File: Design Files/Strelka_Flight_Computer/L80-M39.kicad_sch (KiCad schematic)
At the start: 15 parts

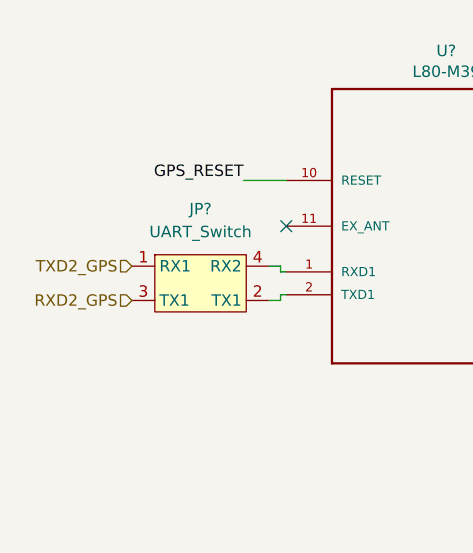
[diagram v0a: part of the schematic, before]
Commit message: Pin mapping and created STM32 .ioc for reference
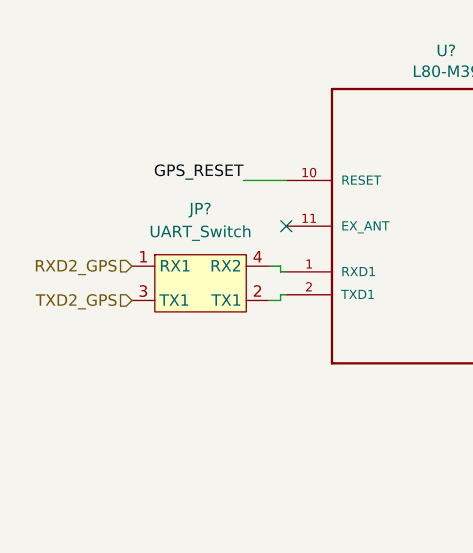
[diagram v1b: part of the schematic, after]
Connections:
- net RXD2_GPS: now also JP?.1 (RX1); no longer JP?.3 (TX1)
- net TXD2_GPS: now also JP?.3 (TX1); no longer JP?.1 (RX1)
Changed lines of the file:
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@@
     (effects (font (size 1.27 1.27)) (justify right bottom))
   )
-  (hierarchical_label "RXD2_GPS" (shape input) (at 85.725 91.44 180)
+  (hierarchical_label "RXD2_GPS" (shape input) (at 85.725 87.63 180)
     (effects (font (size 1.27 1.27)) (justify right))
   )
@@
     (effects (font (size 1.27 1.27)) (justify left))
   )
-  (hierarchical_label "TXD2_GPS" (shape input) (at 85.725 87.63 180)
+  (hierarchical_label "TXD2_GPS" (shape input) (at 85.725 91.44 180)
     (effects (font (size 1.27 1.27)) (justify right))
   )

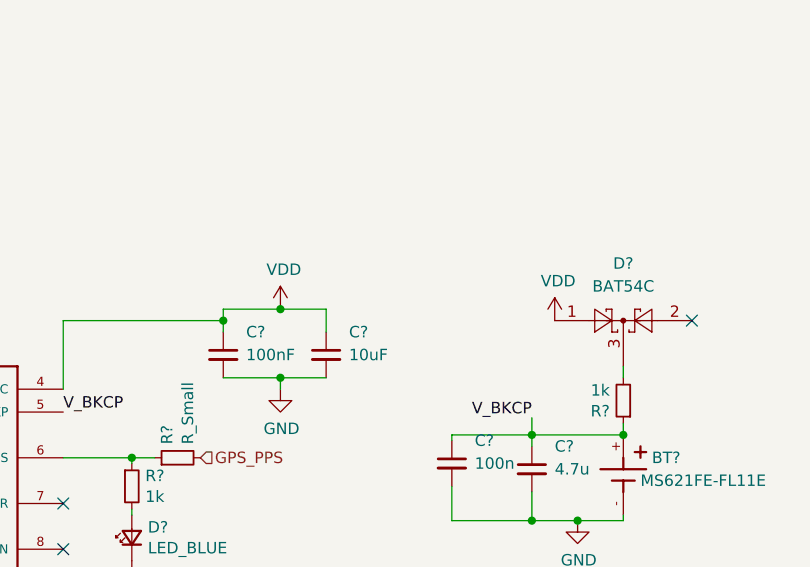
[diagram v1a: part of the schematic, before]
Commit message: Added new UBLOX GPS
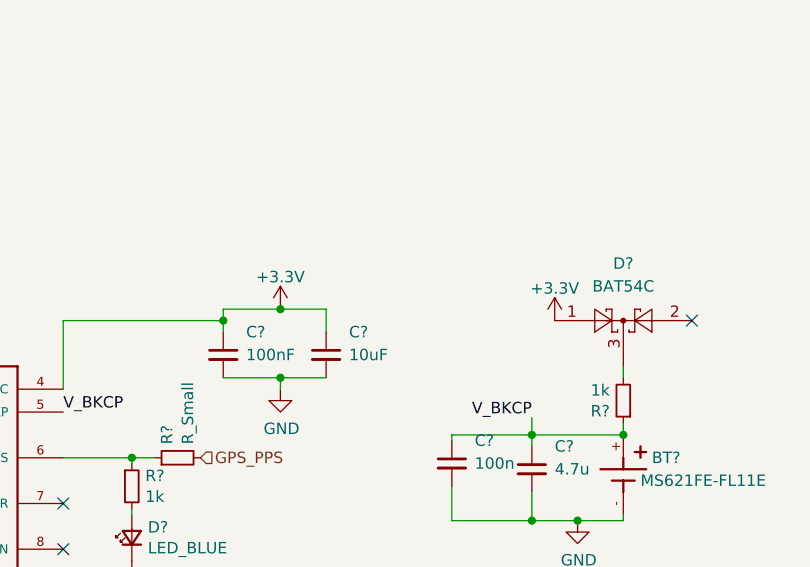
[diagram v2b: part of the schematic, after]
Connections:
- net VDD renamed +3V3
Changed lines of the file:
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@@
   (junction (at 195.58 85.09) (diameter 0) (color 0 0 0 0)
   )
+  (junction (at 190.5 75.565) (diameter 0) (color 0 0 0 0)
+  )
   (junction (at 162.56 61.595) (diameter 0) (color 0 0 0 0)
-  )
-  (junction (at 190.5 75.565) (diameter 0) (color 0 0 0 0)
   )
   (junction (at 184.785 104.775) (diameter 0) (color 0 0 0 0)
@@
     (stroke (width 0) (type default) (color 0 0 0 0))
   )
-  (wire (pts (xy 167.64 61.595) (xy 162.56 61.595))
+  (wire (pts (xy 156.21 61.595) (xy 162.56 61.595))
+    (stroke (width 0) (type default) (color 0 0 0 0))
+  )
+  (wire (pts (xy 162.56 61.595) (xy 167.64 61.595))
     (stroke (width 0) (type default) (color 0 0 0 0))
   )
@@
   )
   (wire (pts (xy 190.5 73.66) (xy 190.5 75.565))
-    (stroke (width 0) (type default) (color 0 0 0 0))
-  )
-  (wire (pts (xy 162.56 61.595) (xy 156.21 61.595))
     (stroke (width 0) (type default) (color 0 0 0 0))
   )
@@
     (effects (font (size 1.27 1.27)) (justify right))
   )
-  (symbol (lib_id "power:VDD") (at 193.04 62.865 0) (unit 1)
-    (in_bom yes) (on_board yes)
+  (symbol (lib_id "power:+3.3V") (at 193.04 62.865 0) (unit 1)
+    (in_bom yes) (on_board yes) (fields_autoplaced)
     (property "Reference" "#PWR?" (id 0) (at 193.04 66.675 0)
       (effects (font (size 1.27 1.27)) hide)
     )
-    (property "Value" "VDD" (id 1) (at 193.421 58.4708 0))
+    (property "Value" "+3.3V" (id 1) (at 193.04 59.2892 0))
     (property "Footprint" "" (id 2) (at 193.04 62.865 0)
       (effects (font (size 1.27 1.27)) hide)
@@
     (pin "1")
   )
-  (symbol (lib_id "Diode:BAT54C") (at 200.66 62.865 0) (unit 1)
+  (symbol (lib_id "Diode:BAT54C") (at 200.66 62.865 0)
     (in_bom yes) (on_board yes) (fields_autoplaced)
     (property "Reference" "D?" (id 0) (at 200.66 56.515 0))
@@
     (pin "3")
   )
-  (symbol (lib_id "Device:R_Small") (at 184.785 108.585 0) (unit 1)
+  (symbol (lib_id "Device:R_Small") (at 184.785 108.585 0)
     (in_bom yes) (on_board yes)
     (property "Reference" "R?" (id 0) (at 186.2836 107.4166 0)
@@
     (pin "2")
   )
-  (symbol (lib_id "Device:LED_Small") (at 146.05 86.995 90) (unit 1)
+  (symbol (lib_id "Device:LED_Small") (at 146.05 86.995 90)
     (in_bom yes) (on_board yes)
     (property "Reference" "D?" (id 0) (at 147.828 85.8266 90)
@@
     (pin "2")
   )
-  (symbol (lib_id "Device:C_Small") (at 167.64 66.675 0) (unit 1)
+  (symbol (lib_id "Device:C_Small") (at 167.64 66.675 0)
     (in_bom yes) (on_board yes)
     (property "Reference" "C?" (id 0) (at 170.18 64.135 0)
@@
     (pin "2")
   )
-  (symbol (lib_id "power:VDD") (at 162.56 61.595 0) (unit 1)
-    (in_bom yes) (on_board yes)
-    (property "Reference" "#PWR?" (id 0) (at 162.56 65.405 0)
-      (effects (font (size 1.27 1.27)) hide)
-    )
-    (property "Value" "VDD" (id 1) (at 162.941 57.2008 0))
-    (property "Footprint" "" (id 2) (at 162.56 61.595 0)
-      (effects (font (size 1.27 1.27)) hide)
-    )
-    (property "Datasheet" "" (id 3) (at 162.56 61.595 0)
-      (effects (font (size 1.27 1.27)) hide)
-    )
-    (pin "1")
-  )
-  (symbol (lib_id "power:GND") (at 162.56 70.485 0) (unit 1)
+  (symbol (lib_id "power:GND") (at 162.56 70.485 0)
     (in_bom yes) (on_board yes)
     (property "Reference" "#PWR?" (id 0) (at 162.56 76.835 0)
@@
     (pin "1")
   )
-  (symbol (lib_id "Device:R_Small") (at 200.66 71.755 180) (unit 1)
+  (symbol (lib_id "Device:R_Small") (at 200.66 71.755 180)
     (in_bom yes) (on_board yes)
     (property "Reference" "R?" (id 0) (at 199.1614 72.9234 0)
@@
     (pin "2")
   )
-  (symbol (lib_id "power:GND") (at 140.97 95.885 0) (unit 1)
+  (symbol (lib_id "power:+3.3V") (at 162.56 61.595 0) (unit 1)
+    (in_bom yes) (on_board yes) (fields_autoplaced)
+    (property "Reference" "#PWR?" (id 0) (at 162.56 65.405 0)
+      (effects (font (size 1.27 1.27)) hide)
+    )
+    (property "Value" "+3.3V" (id 1) (at 162.56 58.0192 0))
+    (property "Footprint" "" (id 2) (at 162.56 61.595 0)
+      (effects (font (size 1.27 1.27)) hide)
+    )
+    (property "Datasheet" "" (id 3) (at 162.56 61.595 0)
+      (effects (font (size 1.27 1.27)) hide)
+    )
+    (pin "1")
+  )
+  (symbol (lib_id "power:GND") (at 140.97 95.885 0)
     (in_bom yes) (on_board yes)
     (property "Reference" "#PWR?" (id 0) (at 140.97 102.235 0)
@@
     (pin "1")
   )
-  (symbol (lib_id "power:GND") (at 146.05 89.535 0) (unit 1)
+  (symbol (lib_id "power:GND") (at 146.05 89.535 0)
     (in_bom yes) (on_board yes)
     (property "Reference" "#PWR?" (id 0) (at 146.05 95.885 0)
@@
     (pin "1")
   )
-  (symbol (lib_id "Device:R_Small") (at 182.245 104.775 90) (unit 1)
+  (symbol (lib_id "Device:R_Small") (at 182.245 104.775 90)
     (in_bom yes) (on_board yes)
     (property "Reference" "R?" (id 0) (at 181.0766 103.2764 0)
@@
     (pin "2")
   )
-  (symbol (lib_id "UART_Switch:UART_Switch") (at 93.345 90.17 0) (unit 1)
+  (symbol (lib_id "UART_Switch:UART_Switch") (at 93.345 90.17 0)
     (in_bom yes) (on_board yes) (fields_autoplaced)
     (property "Reference" "JP?" (id 0) (at 93.345 81.28 0))
@@
     (pin "4")
   )
-  (symbol (lib_id "Device:R_Small") (at 146.05 81.28 0) (unit 1)
+  (symbol (lib_id "Device:R_Small") (at 146.05 81.28 0)
     (in_bom yes) (on_board yes)
     (property "Reference" "R?" (id 0) (at 147.5486 80.1116 0)
@@
     (pin "2")
   )
-  (symbol (lib_id "Device:C_Small") (at 190.5 79.375 0) (unit 1)
+  (symbol (lib_id "Device:C_Small") (at 190.5 79.375 0)
     (in_bom yes) (on_board yes)
     (property "Reference" "C?" (id 0) (at 193.04 76.835 0)
@@
     (pin "2")
   )
-  (symbol (lib_id "Device:C_Small") (at 156.21 66.675 0) (unit 1)
+  (symbol (lib_id "Device:C_Small") (at 156.21 66.675 0)
     (in_bom yes) (on_board yes)
     (property "Reference" "C?" (id 0) (at 158.75 64.135 0)
@@
     (pin "2")
   )
-  (symbol (lib_id "Device:Q_NPN_BCE") (at 193.04 104.775 0) (unit 1)
+  (symbol (lib_id "Device:Q_NPN_BCE") (at 193.04 104.775 0)
     (in_bom yes) (on_board yes)
     (property "Reference" "Q?" (id 0) (at 197.8914 105.9434 0)
@@
     (pin "3")
   )
-  (symbol (lib_id "MS621FE-FL11E:MS621FE-FL11E") (at 200.66 80.01 270) (unit 1)
+  (symbol (lib_id "MS621FE-FL11E:MS621FE-FL11E") (at 200.66 80.01 270)
     (in_bom yes) (on_board yes)
     (property "Reference" "BT?" (id 0) (at 203.835 78.105 90)
@@
     (pin "-")
   )
-  (symbol (lib_id "power:GND") (at 195.58 85.09 0) (unit 1)
+  (symbol (lib_id "power:GND") (at 195.58 85.09 0)
     (in_bom yes) (on_board yes)
     (property "Reference" "#PWR?" (id 0) (at 195.58 91.44 0)
@@
     (pin "1")
   )
-  (symbol (lib_id "Device:C_Small") (at 181.61 78.74 0) (unit 1)
+  (symbol (lib_id "Device:C_Small") (at 181.61 78.74 0)
     (in_bom yes) (on_board yes)
     (property "Reference" "C?" (id 0) (at 184.15 76.2 0)
@@
     (pin "2")
   )
-  (symbol (lib_id "L2_board-rescue:L80-M39-L80-M39") (at 120.65 83.185 0) (unit 1)
+  (symbol (lib_id "L2_board-rescue:L80-M39-L80-M39") (at 120.65 83.185 0)
     (in_bom yes) (on_board yes)
     (property "Reference" "U?" (id 0) (at 120.65 63.7032 0))
@@
     (pin "8")
   )
-  (symbol (lib_id "Device:R_Small") (at 151.13 78.105 90) (unit 1)
+  (symbol (lib_id "Device:R_Small") (at 151.13 78.105 90)
     (in_bom yes) (on_board yes)
     (property "Reference" "R?" (id 0) (at 149.9616 76.6064 0)
@@
     (pin "2")
   )
-  (symbol (lib_id "power:GND") (at 195.58 111.76 0) (unit 1)
+  (symbol (lib_id "power:GND") (at 195.58 111.76 0)
     (in_bom yes) (on_board yes)
     (property "Reference" "#PWR?" (id 0) (at 195.58 118.11 0)

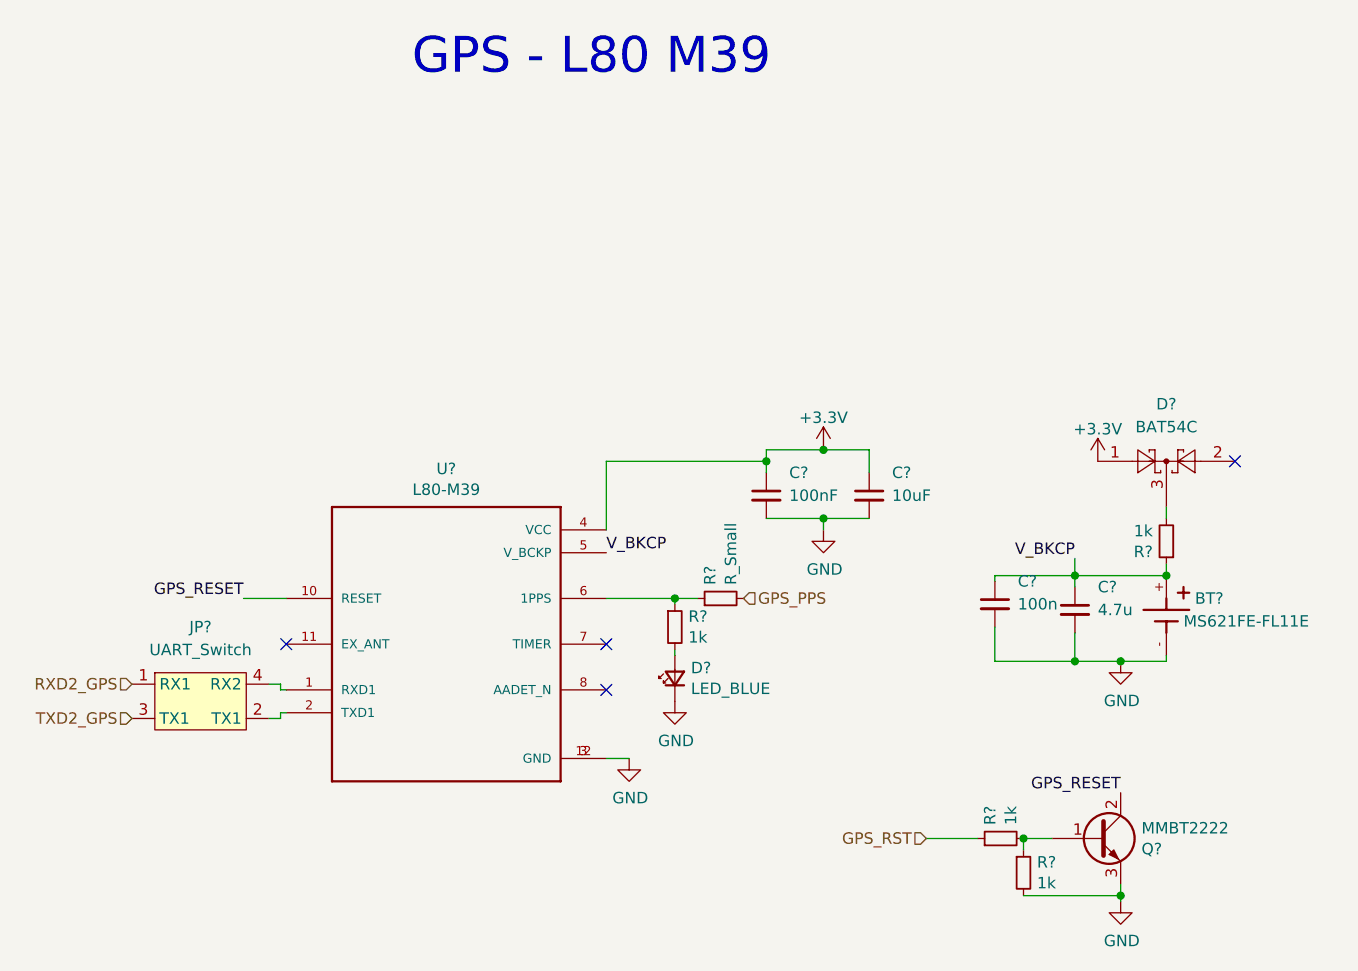
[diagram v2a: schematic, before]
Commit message: Added motor driver to power board
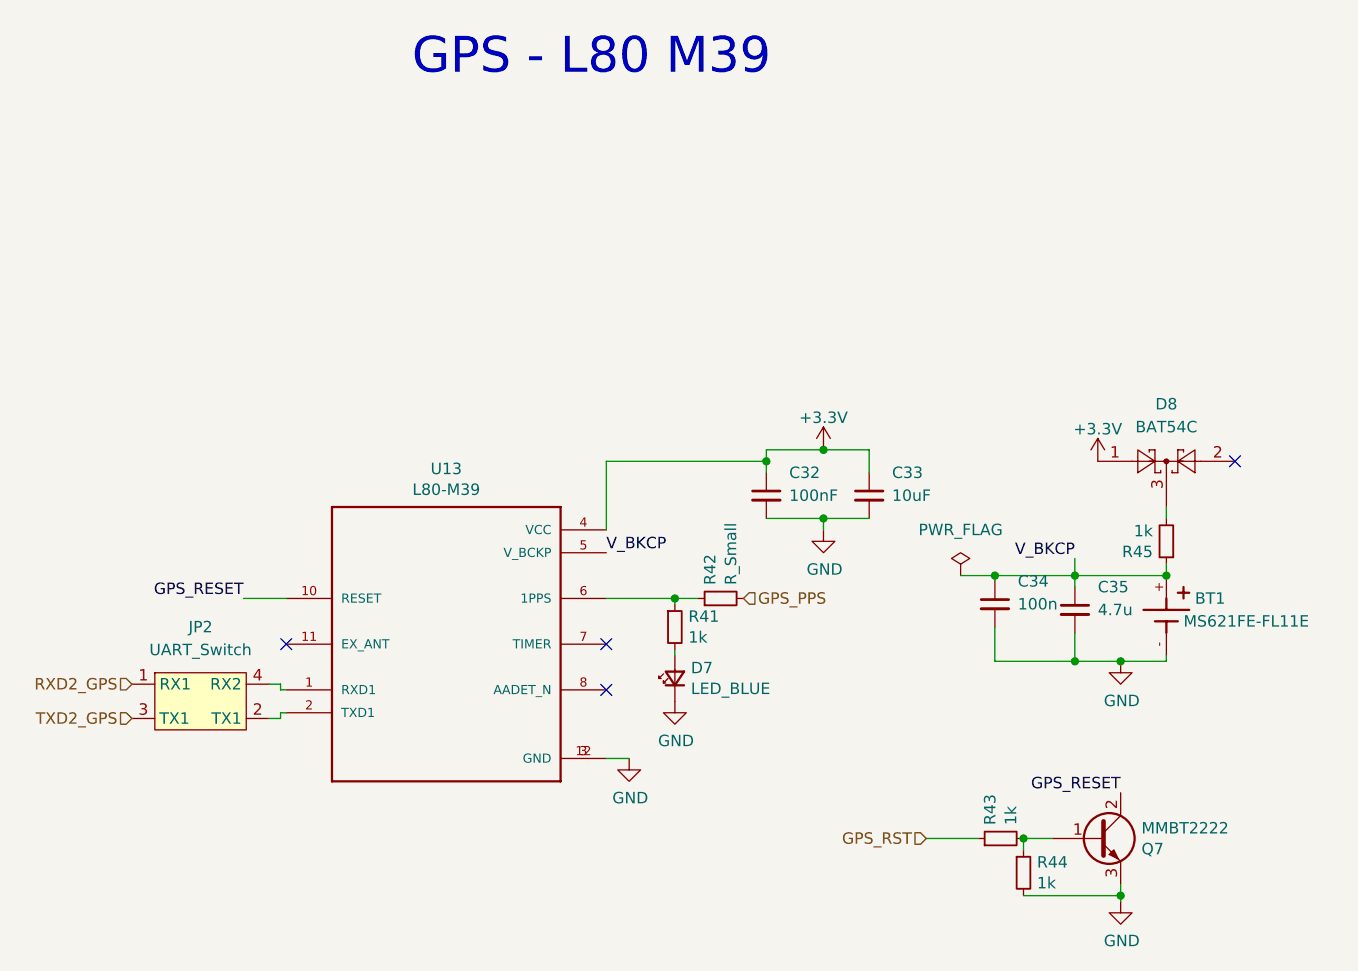
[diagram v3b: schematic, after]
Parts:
- JP2: renamed from JP?; footprint (none) -> Footprints:UART_Switch
- gave numbers to parts that had none: 14

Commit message: Changed boost converter
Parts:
- BT1: footprint BAT_MS621FE-FL11E -> Footprints:BAT_MS621FE-FL11E
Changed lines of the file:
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@@
       (effects (font (size 1.27 1.27)) (justify left))
     )
-    (property "Footprint" "BAT_MS621FE-FL11E" (id 2) (at 204.47 78.74 0)
+    (property "Footprint" "Footprints:BAT_MS621FE-FL11E" (id 2) (at 204.47 78.74 0)
       (effects (font (size 1.27 1.27)) (justify left bottom) hide)
     )
